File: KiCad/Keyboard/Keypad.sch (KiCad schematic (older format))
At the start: 104 parts, among them P1 CONN_6, SW1 MX, SW10 MX, SW11 MX, SW12 MX, SW13 MX, SW14 MX, SW15 MX, SW16 MX, SW17 MX, SW18 MX, SW19 MX, SW2 MX, SW20 MX, SW21 MX, SW22 MX, SW23 MX, SW24 MX, SW25 MX, SW26 MX, SW27 MX, SW28 MX, SW29 MX, SW3 MX, SW30 MX, SW31 MX, SW32 MX, SW33 MX, SW34 MX, SW35 MX, SW36 MX, SW37 MX, SW38 MX, SW39 MX, SW4 MX, SW40 MX, SW41 MX, SW42 MX, SW43 MX, SW44 MX, SW45 MX, SW46 MX, SW47 MX, SW48 MX, SW49 MX, SW5 MX, SW6 MX, SW7 MX, SW8 MX, SW9 MX, U1 TCA8418

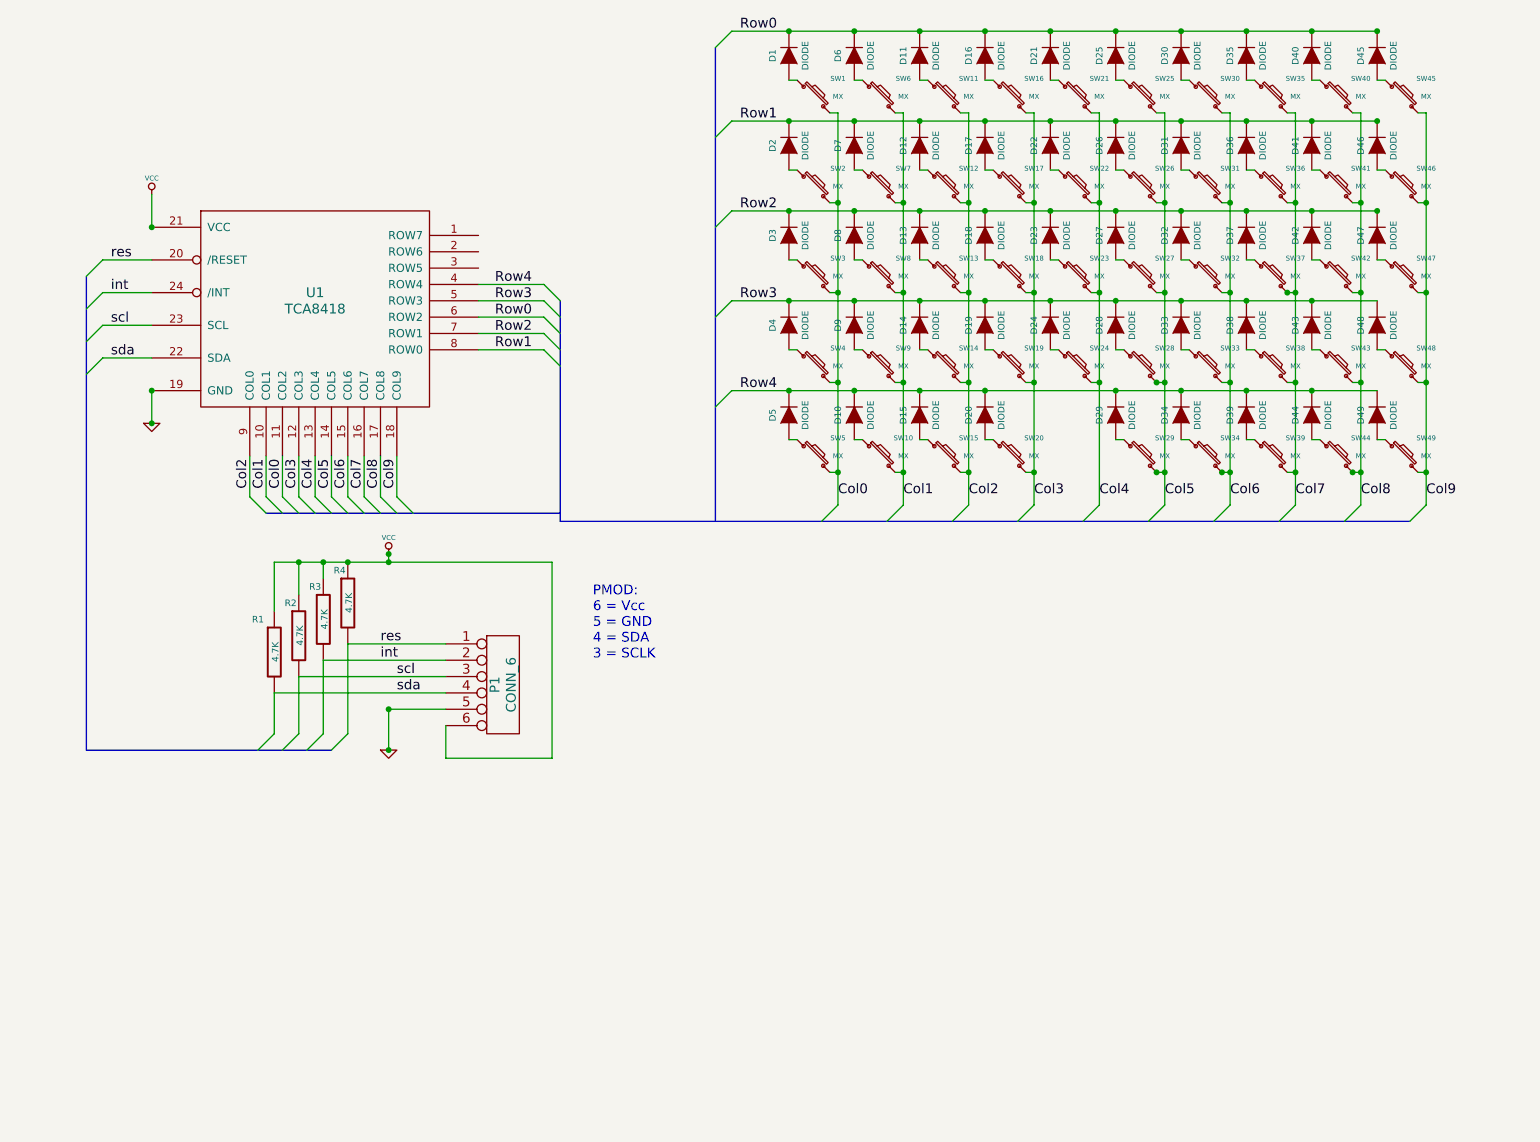
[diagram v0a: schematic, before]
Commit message: Update for 10cm x 5cm PCB
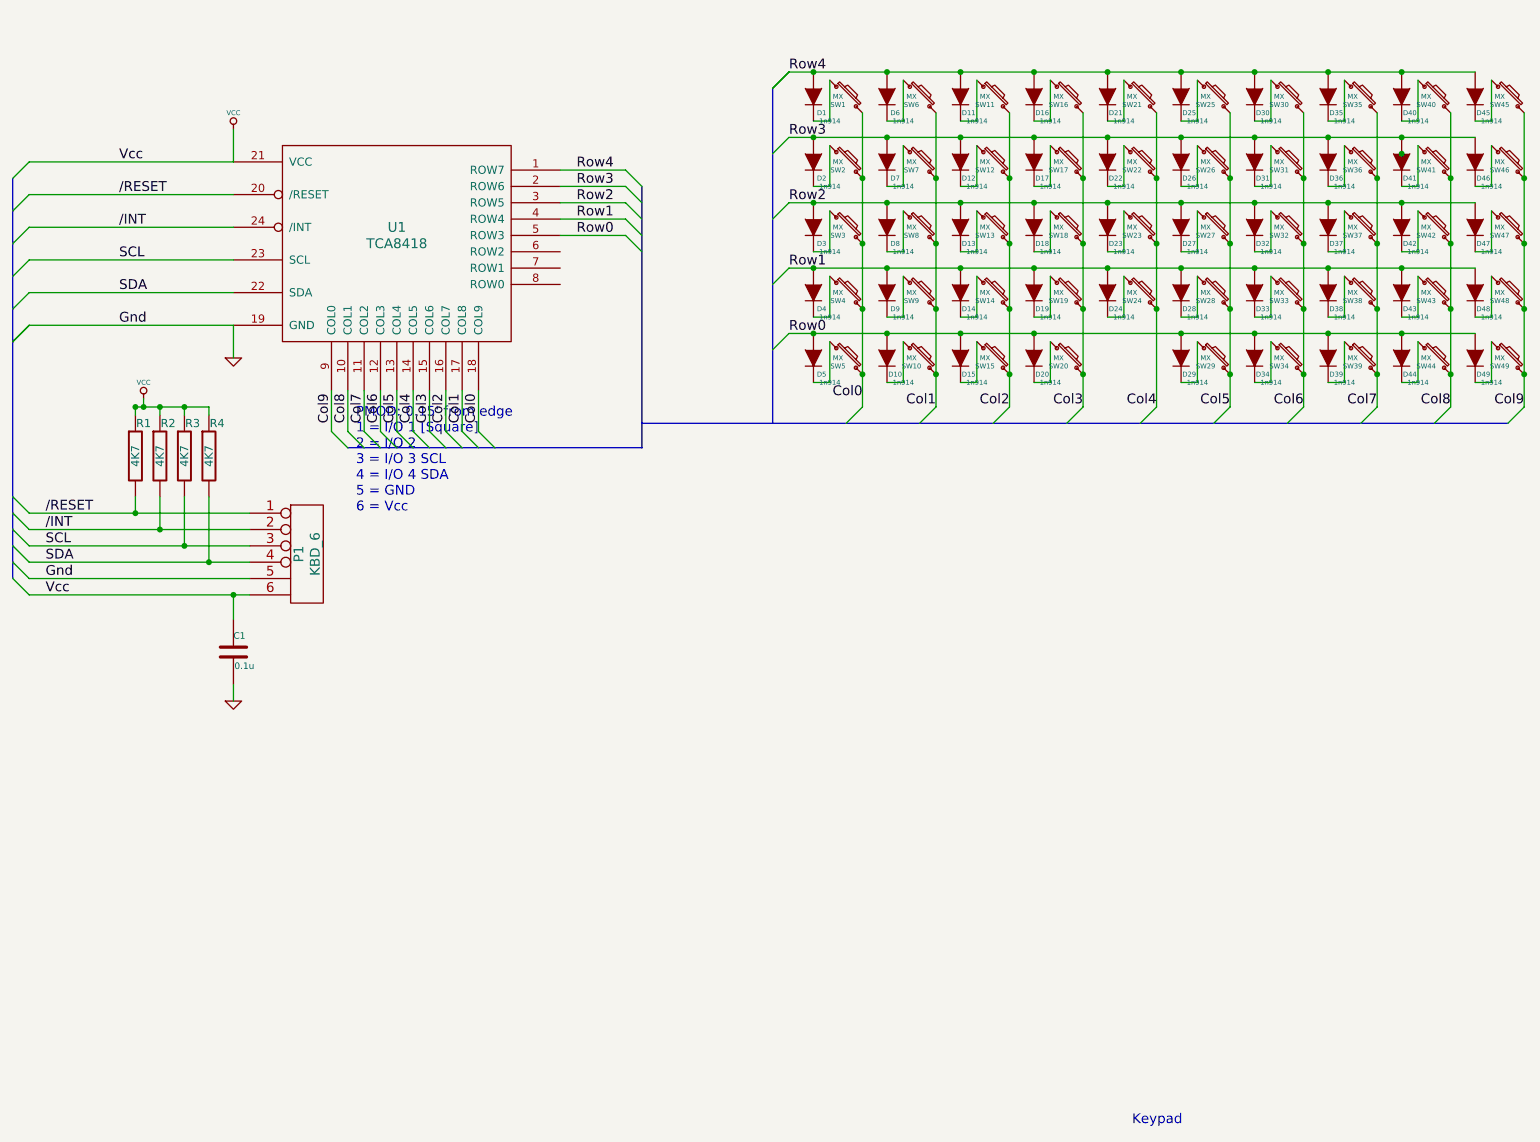
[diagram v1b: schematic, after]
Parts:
- removed P1: CONN_6, symbol CONN_6
- added C1: 0.1u, ~, symbol C
- added P1: KBD_6, symbol KBD_6
- D1, D10, D11, D12, D13, D14, D15, D16, D17, D18, D19, D2, D20, D21, D22, D23, D24, D25, D26, D27, D28, D29, D3, D30, D31, D32, D33, D34, D35, D36, D37, D38, D39, D4, D40, D41, D42, D43, D44, D45, D46, D47, D48, D49, D5, D6, D7, D8, D9: value DIODE -> 1n914; footprint ~ -> (none)
- R1, R2, R3, R4: value 4.7K -> 4K7; footprint ~ -> (none)
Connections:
- net Col0: now also U1.18 (COL9); no longer U1.11 (COL2)
- net Col1: now also U1.17 (COL8); no longer U1.10 (COL1)
- net Col2: now also U1.16 (COL7); no longer U1.9 (COL0)
- net Col3: now also U1.15 (COL6); no longer U1.12 (COL3)
- net Col4: now also U1.14 (COL5); no longer U1.13 (COL4)
- net Col5: now also U1.13 (COL4); no longer U1.14 (COL5)
- net Col6: now also U1.12 (COL3); no longer U1.15 (COL6)
- net Col7: now also U1.11 (COL2); no longer U1.16 (COL7)
- net Col8: now also U1.10 (COL1); no longer U1.17 (COL8)
- net Col9: now also U1.9 (COL0); no longer U1.18 (COL9)
- net GND: now also C1.2, P1.5
- net Row0: now also D10.1 (A), D15.1 (A), D20.1 (A), D29.1 (A), D34.1 (A), D39.1 (A), D44.1 (A), D49.1 (A), D5.1 (A), U1.5 (ROW3); no longer D1.2 (K), D11.2 (K), D16.2 (K), D21.2 (K), D25.2 (K), D30.2 (K), D35.2 (K), D40.2 (K), D45.2 (K), D6.2 (K), U1.6 (ROW2)
- net Row1: now also D14.1 (A), D19.1 (A), D24.1 (A), D28.1 (A), D33.1 (A), D38.1 (A), D4.1 (A), D43.1 (A), D48.1 (A), D9.1 (A), U1.4 (ROW4); no longer D12.2 (K), D17.2 (K), D2.2 (K), D22.2 (K), D26.2 (K), D31.2 (K), D36.2 (K), D41.2 (K), D46.2 (K), D7.2 (K), U1.8 (ROW0)
- net Row2: now also D13.1 (A), D18.1 (A), D23.1 (A), D27.1 (A), D3.1 (A), D32.1 (A), D37.1 (A), D42.1 (A), D47.1 (A), D8.1 (A), U1.3 (ROW5); no longer D13.2 (K), D18.2 (K), D23.2 (K), D27.2 (K), D3.2 (K), D32.2 (K), D37.2 (K), D42.2 (K), D47.2 (K), D8.2 (K), U1.7 (ROW1)
- net Row3: now also D12.1 (A), D17.1 (A), D2.1 (A), D22.1 (A), D26.1 (A), D31.1 (A), D36.1 (A), D41.1 (A), D46.1 (A), D7.1 (A), U1.2 (ROW6); no longer D14.2 (K), D19.2 (K), D24.2 (K), D28.2 (K), D33.2 (K), D38.2 (K), D4.2 (K), D43.2 (K), D48.2 (K), D9.2 (K), U1.5 (ROW3)
- net Row4: now also D1.1 (A), D11.1 (A), D16.1 (A), D21.1 (A), D25.1 (A), D30.1 (A), D35.1 (A), D40.1 (A), D45.1 (A), D6.1 (A), U1.1 (ROW7); no longer D10.2 (K), D15.2 (K), D20.2 (K), D29.2 (K), D34.2 (K), D39.2 (K), D44.2 (K), D49.2 (K), D5.2 (K), U1.4 (ROW4)
- net VCC: now also C1.1, P1.6
- net at SW1.1: now also D1.2 (K); no longer D1.1 (A)
- net at SW2.1: now also D2.2 (K); no longer D2.1 (A)
- net at SW3.1: now also D3.2 (K); no longer D3.1 (A)
- net at SW4.1: now also D4.2 (K); no longer D4.1 (A)
- net at SW6.1: now also D6.2 (K); no longer D6.1 (A)
- net at SW7.1: now also D7.2 (K); no longer D7.1 (A)
- net at SW8.1: now also D8.2 (K); no longer D8.1 (A)
- net at SW9.1: now also D9.2 (K); no longer D9.1 (A)
- net at SW5.1: now also D5.2 (K); no longer D5.1 (A)
- net at SW10.1: now also D10.2 (K); no longer D10.1 (A)
- net at SW11.1: now also D11.2 (K); no longer D11.1 (A)
- net at SW12.1: now also D12.2 (K); no longer D12.1 (A)
- net at SW13.1: now also D13.2 (K); no longer D13.1 (A)
- net at SW14.1: now also D14.2 (K); no longer D14.1 (A)
- net at SW16.1: now also D16.2 (K); no longer D16.1 (A)
- net at SW17.1: now also D17.2 (K); no longer D17.1 (A)
- net at SW18.1: now also D18.2 (K); no longer D18.1 (A)
- net at SW19.1: now also D19.2 (K); no longer D19.1 (A)
- net at SW15.1: now also D15.2 (K); no longer D15.1 (A)
- net at SW20.1: now also D20.2 (K); no longer D20.1 (A)
- net at SW21.1: now also D21.2 (K); no longer D21.1 (A)
- net at SW22.1: now also D22.2 (K); no longer D22.1 (A)
- net at SW23.1: now also D23.2 (K); no longer D23.1 (A)
- net at SW24.1: now also D24.2 (K); no longer D24.1 (A)
- net at SW25.1: now also D25.2 (K); no longer D25.1 (A)
- net at SW26.1: now also D26.2 (K); no longer D26.1 (A)
- net at SW27.1: now also D27.2 (K); no longer D27.1 (A)
- net at SW28.1: now also D28.2 (K); no longer D28.1 (A)
- net at SW29.1: now also D29.2 (K); no longer D29.1 (A)
- net at SW30.1: now also D30.2 (K); no longer D30.1 (A)
- net at SW31.1: now also D31.2 (K); no longer D31.1 (A)
- net at SW32.1: now also D32.2 (K); no longer D32.1 (A)
- net at SW33.1: now also D33.2 (K); no longer D33.1 (A)
- net at SW35.1: now also D35.2 (K); no longer D35.1 (A)
- net at SW36.1: now also D36.2 (K); no longer D36.1 (A)
- net at SW37.1: now also D37.2 (K); no longer D37.1 (A)
- net at SW38.1: now also D38.2 (K); no longer D38.1 (A)
- net at SW34.1: now also D34.2 (K); no longer D34.1 (A)
- net at SW39.1: now also D39.2 (K); no longer D39.1 (A)
- net at SW40.1: now also D40.2 (K); no longer D40.1 (A)
- net at SW41.1: now also D41.2 (K); no longer D41.1 (A)
- net at SW42.1: now also D42.2 (K); no longer D42.1 (A)
- net at SW43.1: now also D43.2 (K); no longer D43.1 (A)
- net at SW45.1: now also D45.2 (K); no longer D45.1 (A)
- net at SW46.1: now also D46.2 (K); no longer D46.1 (A)
- net at SW47.1: now also D47.2 (K); no longer D47.1 (A)
- net at SW48.1: now also D48.2 (K); no longer D48.1 (A)
- net at SW44.1: now also D44.2 (K); no longer D44.1 (A)
- net at SW49.1: now also D49.2 (K); no longer D49.1 (A)
- net int renamed /INT
- net /INT: now also R2.2, P1.2; no longer R3.2
- net res renamed /RESET
- net /RESET: now also R1.2, P1.1; no longer R4.2
- net scl renamed SCL
- net SCL: now also R3.2, P1.3; no longer R2.2
- net sda renamed SDA
- net SDA: now also R4.2, P1.4; no longer R1.2
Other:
- note added: "Keypad"
- note added: "PMOD: 0.15' from edge\n1 = I/O 1 [Square]\n2 = I/O 2\n3 = I/O 3 SCL\n4 = I/O 4 SDA\n5 = GND\n6 = Vcc"
- note removed: "PMOD:\n6 = Vcc\n5 = GND\n4 = SDA\n3 = SCLK"
- moved on the sheet: SW1, U1
